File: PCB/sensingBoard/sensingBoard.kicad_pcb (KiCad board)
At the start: 2 copper layers, 38 x 38 mm, 37 parts, among them J1 Conn_01x02_Socket, J2 Conn_01x03_Socket, J4 Conn_01x04_MountingPin, P1 USB_C_Plug_USB2.0, U1 AMS1117, U2 ESP32-C3-MINI-1, X1 32.768

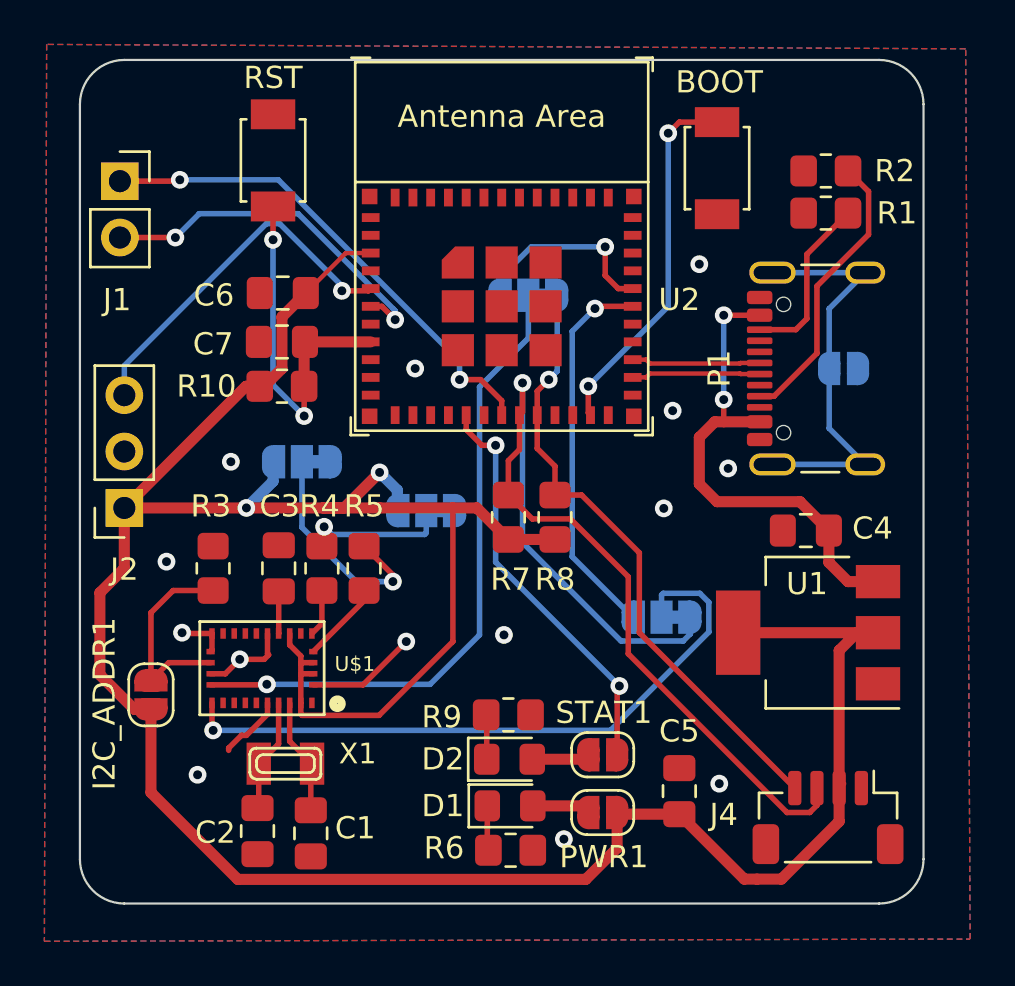
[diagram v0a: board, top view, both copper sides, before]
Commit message: modified sensor board and wrote firmware for wireless data transfer
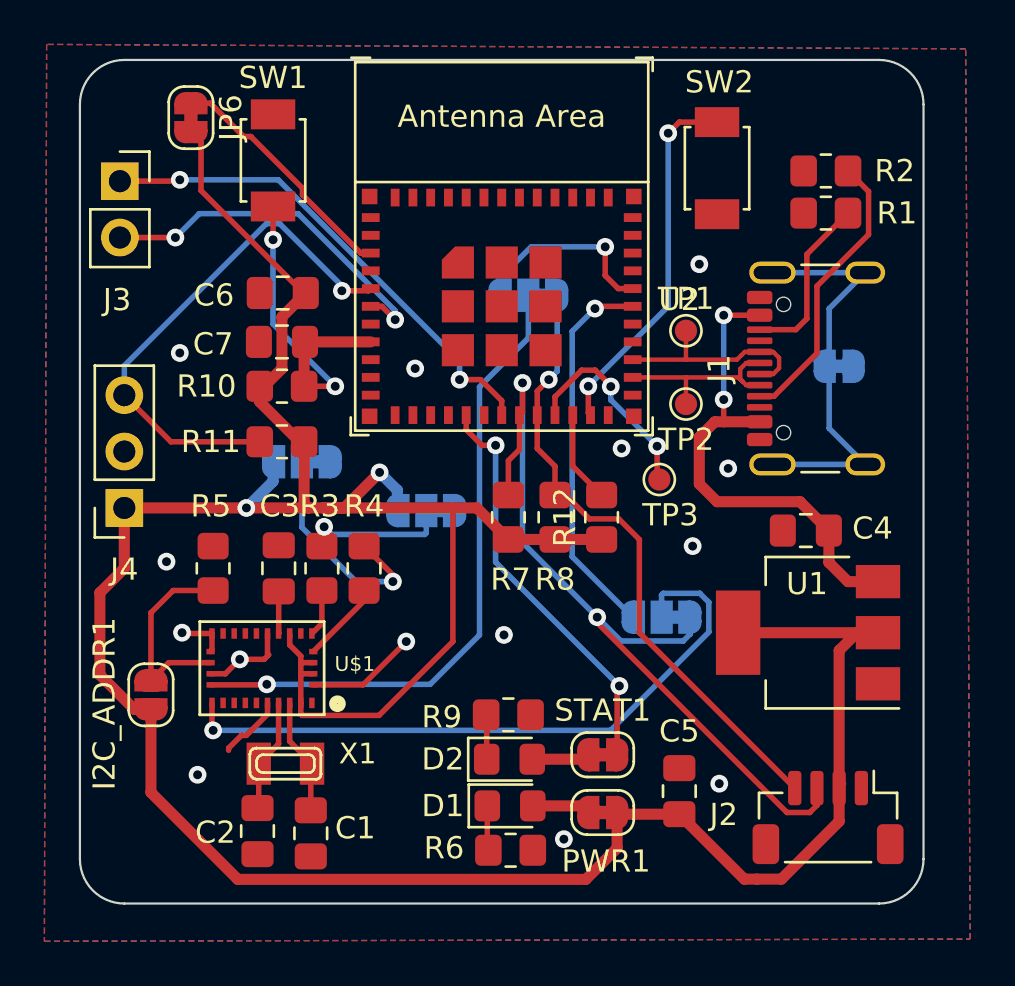
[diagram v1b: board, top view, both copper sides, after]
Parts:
- removed P1: USB_C_Plug_USB2.0, Connector_USB:USB_C_Receptacle_GCT_USB4105-xx-A_16P_TopMnt_Horizontal
- added J1: USB_C_Receptacle_USB2.0_14P, Connector_USB:USB_C_Receptacle_GCT_USB4105-xx-A_16P_TopMnt_Horizontal, F.Cu at (84.3, 63.9)
- added JP6: ~, Jumper:SolderJumper-2_P1.3mm_Bridged_RoundedPad1.0x1.5mm, F.Cu at (55.0, 52.6)
- added R11: 100k, Resistor_SMD:R_0805_2012Metric_Pad1.20x1.40mm_HandSolder, F.Cu at (59.1, 67.2)
- added R12: 100k, Resistor_SMD:R_0805_2012Metric_Pad1.20x1.40mm_HandSolder, F.Cu at (73.5, 70.6)
- added TP1: TestPoint, TestPoint:TestPoint_Pad_D1.0mm, F.Cu at (77.3, 62.2)
- added TP2: TestPoint, TestPoint:TestPoint_Pad_D1.0mm, F.Cu at (77.3, 65.5)
- added TP3: TestPoint, TestPoint:TestPoint_Pad_D1.0mm, F.Cu at (76.1, 68.9)
- JP1, PWR1, STAT1: footprint Jumper:SolderJumper-2_P1.3mm_Open_RoundedPad1.0x1.5mm -> Jumper:SolderJumper-2_P1.3mm_Bridged_RoundedPad1.0x1.5mm
- moved JP1 0.22 mm to (84.2, 63.8)
- renumbered J4 to J2, J1 to J3, J2 to J4, JP4 to JP3, JP5 to JP4, JP3 to JP5, R4 to R3, R5 to R4, R3 to R5, RST to SW1, BOOT to SW2
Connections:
- U2 pad 21: unconnected-(U2-GPIO7-Pad21) -> Net-(U2-GPIO7)
- U2 pad 22: unconnected-(U2-GPIO8-Pad22) -> Net-(U2-GPIO8)
- U2 pad 3: +3V3 -> Net-(JP6-A)
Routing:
- net Net-(JP6-A): track 0.00 -> 11.1 mm
- net Net-(U2-GPIO7): track 0.00 -> 9.26 mm, vias 0 -> 2
- net SDA: track 45.6 -> 37.4 mm, vias 1 -> 2
- net ADC1-2: track 16.5 -> 23.5 mm
- net +3V3: track 132.5 -> 138.5 mm
- net Net-(U2-GPIO8): track 0.00 -> 4.14 mm
- net USB_P: track 5.80 -> 9.60 mm
- net USB_N: track 5.80 -> 8.64 mm
- net ~{RST}: track 16.3 -> 15.6 mm
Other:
- board text added: "Sensing Board v1.1 Katerina B & Binh-Minh N"
- board text removed: "Sensing Board v1.0 Katerina B & Binh-Minh N"

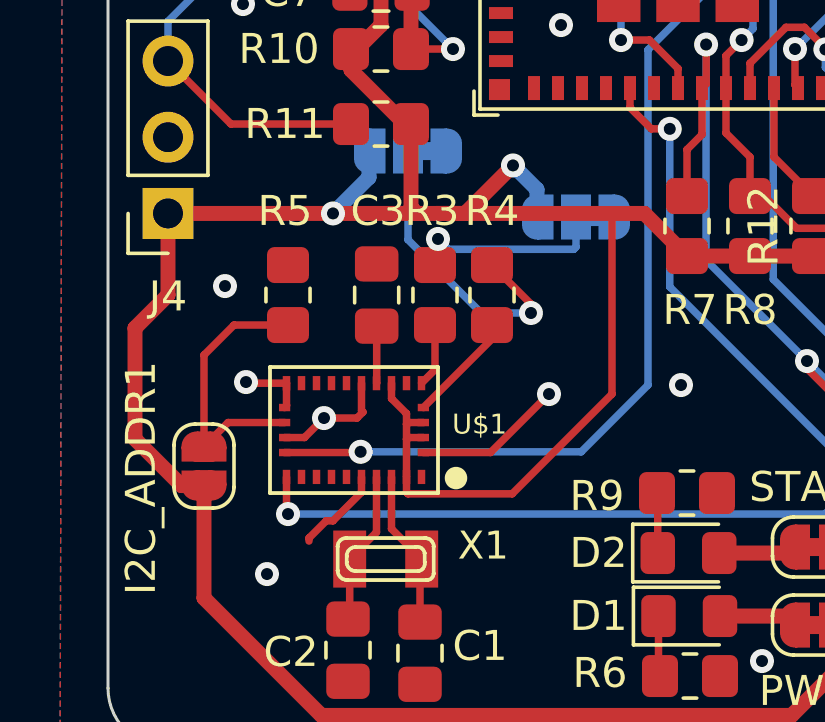
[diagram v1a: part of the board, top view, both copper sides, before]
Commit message: gitignore for kicad backup, added pullup for nreset on imu
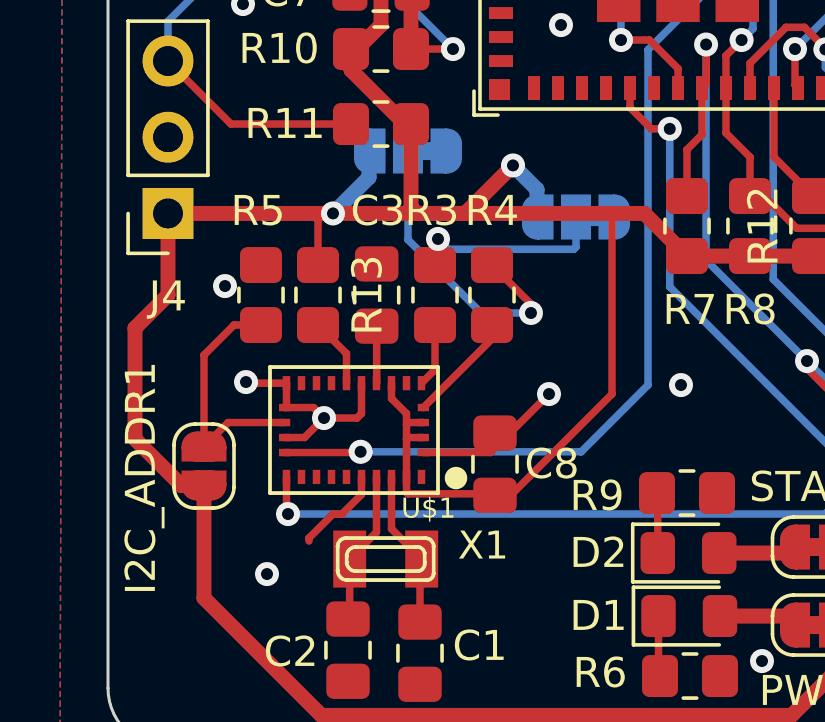
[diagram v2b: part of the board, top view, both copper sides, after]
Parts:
- added C8: 0.1u, Capacitor_SMD:C_0805_2012Metric_Pad1.18x1.45mm_HandSolder, F.Cu at (62.9, 78.5)
- added R13: 10k, Resistor_SMD:R_0805_2012Metric_Pad1.20x1.40mm_HandSolder, F.Cu at (57.0, 72.9)
- moved R5 0.90 mm to (55.1, 72.9)
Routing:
- net /NRESET_3V: track 0.00 -> 2.33 mm
- net +3V3: track 138.5 -> 140.3 mm
- net GND: track 14.2 -> 15.7 mm
- net /I2CADDR_3V: track 9.28 -> 8.38 mm
